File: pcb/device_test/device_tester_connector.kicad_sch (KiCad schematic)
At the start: 8 parts, among them J201 USB_C_Receptacle_USB2.0_16P, J202 Conn_01x04, J203 Conn_02x10_Row_Letter_First

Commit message: upgrade to kicad 9.0.0
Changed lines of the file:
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@@
 (kicad_sch
-	(version 20231120)
+	(version 20250114)
 	(generator "eeschema")
-	(generator_version "8.0")
+	(generator_version "9.0")
 	(paper "A4")
 	(title_block
@@
 			(at 151.13 99.06 0)
 			(effects
+				(font
+					(size 1.27 1.27)
+				)
+				(hide yes)
+			)
+		)
+		(property "Sim.Pins" "1=K 2=A"
+			(at 151.13 99.06 0)
+			(effects

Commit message: update ALL parts
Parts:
- C201: footprint Capacitor_Tantalum_SMD:CP_EIA-7343-43_Kemet-X_Pad2.25x2.55mm_HandSolder -> Capacitor_Tantalum_SMD:CP_EIA-7343-43_Kemet-X; LCSC C7230 -> C132558
- J203: MOUSER (none) -> 798-PCN1020P254DS72
- R203: value 390 -> 1k; LCSC C17655 -> C17513
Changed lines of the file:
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@@
+			)
+		)
+		(property "MOUSER" ""
+			(at 151.13 99.06 0)
+			(effects
+				(font
+					(size 1.27 1.27)
+				)
 			)
 		)
@@
 			)
 		)
+		(property "MOUSER" ""
+			(at 128.27 107.95 0)
+			(effects
+				(font
+					(size 1.27 1.27)
+				)
+			)
+		)
 		(pin "1"
 		)
@@
 			)
 		)
-		(property "Footprint" "Capacitor_Tantalum_SMD:CP_EIA-7343-43_Kemet-X_Pad2.25x2.55mm_HandSolder"
+		(property "Footprint" "Capacitor_Tantalum_SMD:CP_EIA-7343-43_Kemet-X"
 			(at 134.3152 74.93 0)
 			(effects
@@
 			)
 		)
-		(property "LCSC" "C7230"
+		(property "LCSC" "C132558"
 			(at 133.35 71.12 0)
 			(effects
@@
 				)
 				(hide yes)
+			)
+		)
+		(property "MOUSER" ""
+			(at 133.35 71.12 0)
+			(effects
+				(font
+					(size 1.27 1.27)
+				)
 			)
 		)
@@
 			)
 		)
+		(property "MOUSER" ""
+			(at 86.36 97.79 0)
+			(effects
+				(font
+					(size 1.27 1.27)
+				)
+			)
+		)
 		(pin "B1"
 		)
@@
 			)
 		)
+		(property "MOUSER" "798-PCN1020P254DS72"
+			(at 199.39 101.6 0)
+			(effects
+				(font
+					(size 1.27 1.27)
+				)
+			)
+		)
 		(pin "a3"
 		)
@@
 			)
 		)
+		(property "MOUSER" ""
+			(at 139.7 107.95 0)
+			(effects
+				(font
+					(size 1.27 1.27)
+				)
+			)
+		)
 		(pin "1"
 		)
@@
 			)
 		)
-		(property "Value" "390"
+		(property "Value" "1k"
 			(at 153.67 110.4899 0)
 			(effects
@@
 			)
 		)
-		(property "LCSC" "C17655"
+		(property "LCSC" "C17513"
 			(at 151.13 109.22 0)
 			(effects
@@
 				)
 				(hide yes)
+			)
+		)
+		(property "MOUSER" ""
+			(at 151.13 109.22 0)
+			(effects
+				(font
+					(size 1.27 1.27)
+				)
 			)
 		)
@@
 			)
 		)
+		(property "MOUSER" ""
+			(at 167.64 53.34 0)
+			(effects
+				(font
+					(size 1.27 1.27)
+				)
+			)
+		)

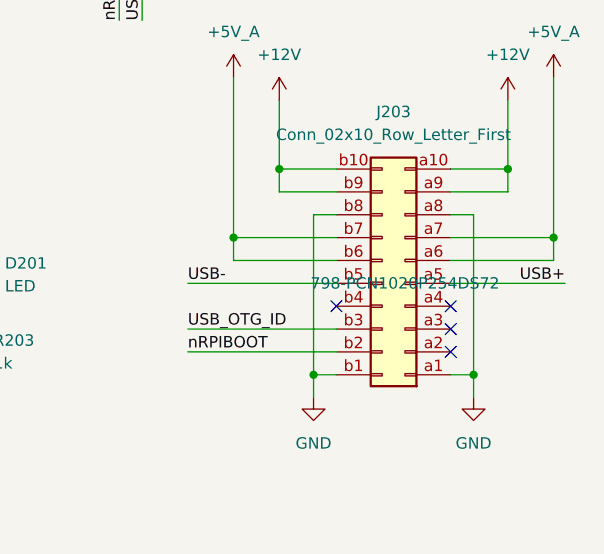
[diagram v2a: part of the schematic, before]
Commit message: fix device tester pcb
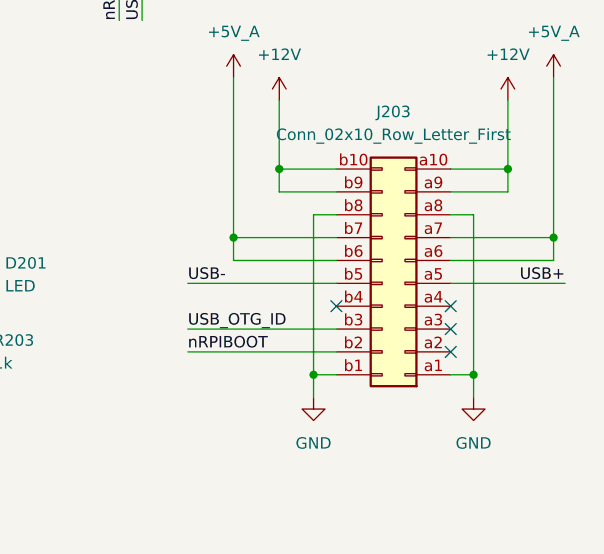
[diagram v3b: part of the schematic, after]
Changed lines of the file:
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@@
 					(size 1.27 1.27)
 				)
+				(hide yes)
 			)
 		)
